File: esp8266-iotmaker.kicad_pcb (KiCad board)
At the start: 2 copper layers, 66.3 x 30.7 mm, 70 parts, among them J1 CONN_01X04, J2 CONN_01X02, J3 CONN_01X08, J4 CONN_01X06, J5 CONN_01X08, J6 CONN_01X04, Q1 S8050, Q2 S8050, SW1 SW_Push, SW2 SW_Push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

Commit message: complete pcb source
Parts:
- removed C19, C20, C21, C22: C, esp8266:C_0603
- C12, C14: value C -> 10uF; footprint esp8266:C_0603 -> Capacitors_SMD:CP_Elec_4x5.3
- C15, C18: value C -> 22uF; footprint esp8266:C_0603 -> Capacitors_SMD:CP_Elec_4x5.3
- D5: footprint esp8266:do214aa-g -> Diodes_SMD:D_SOD-323
- D7: footprint Diodes_SMD:D_SOD-123 -> Diodes_SMD:D_SOD-323
- SW1, SW2: footprint esp8266:Tact_Switch_TS6X3.6 -> esp8266:micro-buttom
- moved D4 76.5 mm to (90.8, 124.1)
- moved L1 68.8 mm to (121.2, 123.0), turned to 0 degrees
- moved C2 68.8 mm to (121.2, 123.0), turned to 0 degrees
- moved C14 67.4 mm to (99.2, 126.4), turned to 90 degrees
- moved C1 67.1 mm to (121.2, 123.0), turned to 0 degrees
- moved L2 65.9 mm to (121.2, 123.0)
- moved C3 65.6 mm to (121.2, 123.0), turned to 0 degrees
- moved R20 65.0 mm to (121.2, 123.0), turned to 0 degrees
- moved C4 64.4 mm to (121.2, 123.0)
- moved R13 64.1 mm to (121.2, 123.0), turned to 0 degrees
- moved C5 63.7 mm to (121.2, 123.0), turned to 0 degrees
- moved Y1 63.7 mm to (121.2, 123.0), turned to 0 degrees
- moved R12 62.5 mm to (121.2, 123.0), turned to 0 degrees
- moved C7 61.3 mm to (121.2, 123.0), turned to 0 degrees
- moved D2 60.3 mm to (121.2, 123.0), turned to 0 degrees
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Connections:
- C14 pad 1: VBAT -> Net-(C14-Pad1)
- C15 pad 1: Net-(C15-Pad1) -> 3V3
- C18 pad 1: Net-(C15-Pad1) -> 5V
- D4 pad 1: Net-(C15-Pad1) -> Net-(C14-Pad1)
- D5 pad 1: Net-(C15-Pad1) -> Net-(C14-Pad1)
- U7 pad 3: Net-(C15-Pad1) -> Net-(C14-Pad1)
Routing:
- net GND: track 325.7 -> 50.3 mm, vias 14 -> 0
- net 3V3: track 174.2 -> 6.35 mm, vias 8 -> 1
- net REST: track 80.4 -> 0.00 mm, vias 1 -> 0
- net GPIO16: track 72.7 -> 0.00 mm, vias 2 -> 0
- net VBAT: track 74.8 -> 4.18 mm, vias 2 -> 0
- net TXD: track 61.7 -> 0.00 mm, vias 2 -> 0
- net GPIO0: track 56.2 -> 0.00 mm, vias 3 -> 0
- net RXD: track 51.7 -> 0.00 mm, vias 2 -> 0
- net EN: track 42.1 -> 0.00 mm, vias 2 -> 0
- net MOSI: track 38.4 -> 0.00 mm, vias 1 -> 0
- net GPIO14: track 37.6 -> 0.00 mm, vias 1 -> 0
- net CSO: track 37.2 -> 0.00 mm, vias 1 -> 0
- net GPIO12: track 34.0 -> 0.00 mm, vias 1 -> 0
- net GPIO13: track 30.8 -> 0.00 mm, vias 1 -> 0
- net GPIO15: track 28.9 -> 0.00 mm, vias 1 -> 0
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- removed copper zone on B.Cu, net GND
- removed copper zone on F.Cu, net GND
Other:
- board size 66.3 x 30.7 mm -> 50.8 x 25.4 mm
- net class Default: trace_width 0.254 -> 0.2; via_dia 1.1 -> 1; via_drill 0.6 -> 0.5

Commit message: xap xep linh kien
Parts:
- removed BT1: Battery, Pin_Headers:Pin_Header_Straight_2x01_Pitch2.00mm
- removed C14: 10uF, Capacitors_SMD:CP_Elec_4x5.3
- removed C16: 4.7uF, esp8266:C_0603
- removed C17: 1uF, esp8266:C_0603
- removed C18: 22uF, Capacitors_SMD:CP_Elec_4x5.3
- removed D2: ZENER_3V3, Diodes_SMD:D_SOD-323_HandSoldering
- removed D4: SS34, esp8266:do214aa-g
- removed D7: BAT60JFILM, Diodes_SMD:D_SOD-323
- removed J3, J5: CONN_01X08, Pin_Headers:Pin_Header_Straight_1x08_Pitch2.54mm
- removed J4: CONN_01X06, Pin_Headers:Pin_Header_Straight_1x06_Pitch2.54mm
- removed J6: CONN_01X04, Pin_Headers:Pin_Header_Straight_1x04_Pitch2.54mm
- removed R17: 2K, esp8266:R_0603
- removed R19: 100k, esp8266:R_0603
- removed U5: mcp73831, TO_SOT_Packages_SMD:SOT-23-5
- removed U7: AMS1117-3.3, TO_SOT_Packages_SMD:SOT-223
- removed U8: MOSFET-P, esp8266:SOT-23_standar
- C12: value 10uF -> 10uF TANT; footprint Capacitors_SMD:CP_Elec_4x5.3 -> Capacitors_SMD:C_1206
- C13: value 4.7uF -> 100nF
- C15: value 22uF -> 10uF TANT; footprint Capacitors_SMD:CP_Elec_4x5.3 -> Capacitors_SMD:C_1206
- D5: value SS34 -> 1n5819; footprint Diodes_SMD:D_SOD-323 -> Diodes_SMD:D_SOD-123
- J1: value CONN_01X04 -> CONN_01X10; footprint Pin_Headers:Pin_Header_Straight_1x04_Pitch2.54mm -> Pin_Headers:Pin_Header_Straight_1x10_Pitch2.54mm
- J2: value CONN_01X02 -> CONN_01X10; footprint Pin_Headers:Pin_Header_Straight_1x02_Pitch2.54mm -> Pin_Headers:Pin_Header_Straight_1x10_Pitch2.54mm
- SW1, SW2: footprint esp8266:micro-buttom -> esp8266:tactile switches
- U3: footprint Housings_DFN_QFN:QFN-28-1EP_5x5mm_Pitch0.5mm -> esp8266:cp2102
- U4: footprint Housings_SOIC:SOIJ-8_5.3x5.3mm_Pitch1.27mm -> Housings_SOIC:SOIC-8_3.9x4.9mm_Pitch1.27mm
- moved R8 60.6 mm to (118.6, 62.5), turned to 180 degrees
- moved R4 59.0 mm to (118.6, 64.0), turned to 180 degrees
- moved R15 57.6 mm to (118.6, 65.5), turned to 180 degrees
- moved R5 56.1 mm to (118.6, 66.9), turned to 180 degrees
- moved C15 51.9 mm to (96.8, 77.2), turned to 180 degrees
- moved L1 50.9 mm to (136.2, 74.3)
- moved D1 50.4 mm to (95.0, 79.9), turned to 270 degrees
- moved R11 49.7 mm to (96.4, 79.9), turned to 270 degrees
- moved C2 49.6 mm to (134.2, 75.1), turned to 90 degrees
- moved R7 49.4 mm to (145.5, 79.9)
- moved L2 49.3 mm to (136.2, 76.0)
- moved C3 49.3 mm to (132.7, 75.1), turned to 90 degrees
- moved C1 49.0 mm to (131.4, 75.1), turned to 90 degrees
- moved R12 48.7 mm to (129.8, 75.1), turned to 270 degrees
- moved R13 48.4 mm to (128.3, 75.1), turned to 90 degrees
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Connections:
- C12 pad 1: VBAT -> VCC
- C13 pad 1: 5V -> 3V3
- C6 pad 1: VUSB -> VCC
- C8 pad 1: VUSB -> VCC
- D5 pad 1: Net-(C14-Pad1) -> VCC
- J1 pad 1: GPIO16 -> GPIO14
- J1 pad 2: ADC_EX -> GPIO12
- J1 pad 3: GND -> GPIO13
- J1 pad 4: 3V3 -> GPIO15
- J2 pad 1: GPIO2 -> GPIO16
- J2 pad 2: GPIO0 -> ADC_EX
- U3 pad 29: (no net) -> GND
- U3 pad 8: VUSB -> VCC
- U4 pad 8: GND -> 3V3
- U6 pad 3: VBAT -> VCC
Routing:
- net GND: track 50.3 -> 16.3 mm, vias 0 -> 1
- net VCC: track 0.00 -> 24.3 mm
- net MOSI: track 0.00 -> 22.2 mm
- net Net-(BT1-Pad1): track 19.0 -> 0.00 mm
- net D-: track 1.05 -> 15.9 mm, vias 1 -> 2
- net D+: track 1.09 -> 15.0 mm, vias 1 -> 2
- net 3V3: track 6.35 -> 18.2 mm, vias 1 -> 0
- net GPIO9: track 0.00 -> 10.6 mm
- net 5V: track 10.1 -> 0.00 mm
- net TXD: track 0.00 -> 9.74 mm
- net RXD: track 0.00 -> 9.68 mm
- net Net-(C7-Pad2): track 0.00 -> 9.32 mm
- net VUSB: track 13.3 -> 4.54 mm
- net Net-(R3-Pad1): track 0.00 -> 8.49 mm
- net MISO: track 0.00 -> 7.89 mm
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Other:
- board outline removed

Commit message: complete pcb ver2.0
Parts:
- SW1, SW2: footprint esp8266:tactile switches -> esp8266:nut_nhan_ngang
- moved R14 40.2 mm to (98.1, 74.8), turned to 270 degrees
- moved C13 39.7 mm to (119.4, 91.6), turned to 90 degrees
- moved R15 32.6 mm to (97.5, 90.4)
- moved R8 24.3 mm to (107.5, 84.0)
- moved R7 21.8 mm to (128.9, 94.1), turned to 270 degrees
- moved R3 20.7 mm to (112.4, 91.4), turned to 270 degrees
- moved C11 18.6 mm to (129.5, 91.0), turned to 90 degrees
- moved AE1 16.6 mm to (129.7, 79.0), turned to 270 degrees
- moved R4 15.7 mm to (109.8, 77.0)
- moved C7 15.2 mm to (122.5, 93.3), turned to 90 degrees
- moved U4 15.0 mm to (116.0, 90.0), turned to 270 degrees
- moved Y1 14.9 mm to (125.0, 93.3), turned to 90 degrees
- moved R6 14.6 mm to (112.9, 79.6), turned to 180 degrees
- moved R5 14.6 mm to (109.8, 78.5)
- moved R12 12.3 mm to (117.9, 78.2)
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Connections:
- J2 pad 1: GPIO16 -> GND
- J2 pad 10: GND -> REST
- J2 pad 2: ADC_EX -> GND
- J2 pad 3: GND -> VCC
- J2 pad 5: EN -> GPIO0
- J2 pad 6: REST -> GPIO2
- J2 pad 7: GPIO0 -> GPIO16
- J2 pad 8: GPIO2 -> EN
- J2 pad 9: VUSB -> ADC_EX
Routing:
- net GND: track 16.3 -> 236.2 mm, vias 1 -> 14
- net 3V3: track 18.2 -> 146.5 mm, vias 0 -> 11
- net REST: track 0.00 -> 101.6 mm, vias 0 -> 5
- net GPIO0: track 1.29 -> 66.8 mm, vias 1 -> 2
- net GPIO16: track 3.23 -> 50.5 mm, vias 0 -> 2
- net GPIO15: track 0.00 -> 46.1 mm, vias 0 -> 1
- net GPIO14: track 0.00 -> 32.4 mm
- net GPIO12: track 0.00 -> 29.3 mm
- net GPIO2: track 0.00 -> 27.8 mm, vias 0 -> 1
- net DTR: track 2.67 -> 28.4 mm, vias 1 -> 0
- net GPIO13: track 0.00 -> 25.5 mm
- net TXD: track 9.74 -> 33.6 mm, vias 0 -> 1
- net GPIO4: track 0.00 -> 23.5 mm, vias 0 -> 1
- net RXD: track 9.68 -> 32.7 mm, vias 0 -> 1
- net EN: track 0.00 -> 17.2 mm
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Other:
- board outline added: 50.8 x 26.2 mm
- net class Default: clearance 0.2 -> 0.254
- rule trace_clearance: 0.2 -> 0.254

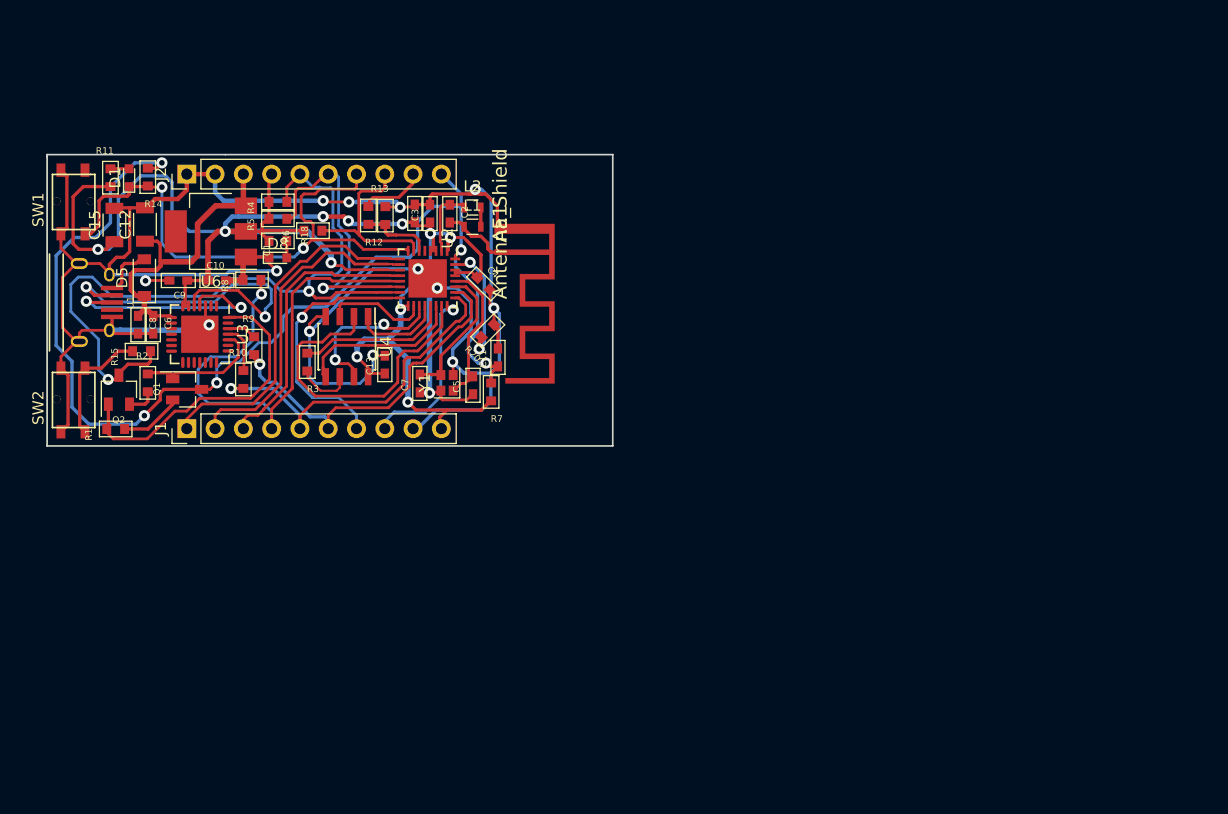
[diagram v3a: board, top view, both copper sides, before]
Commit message: add 3d and edit pcb
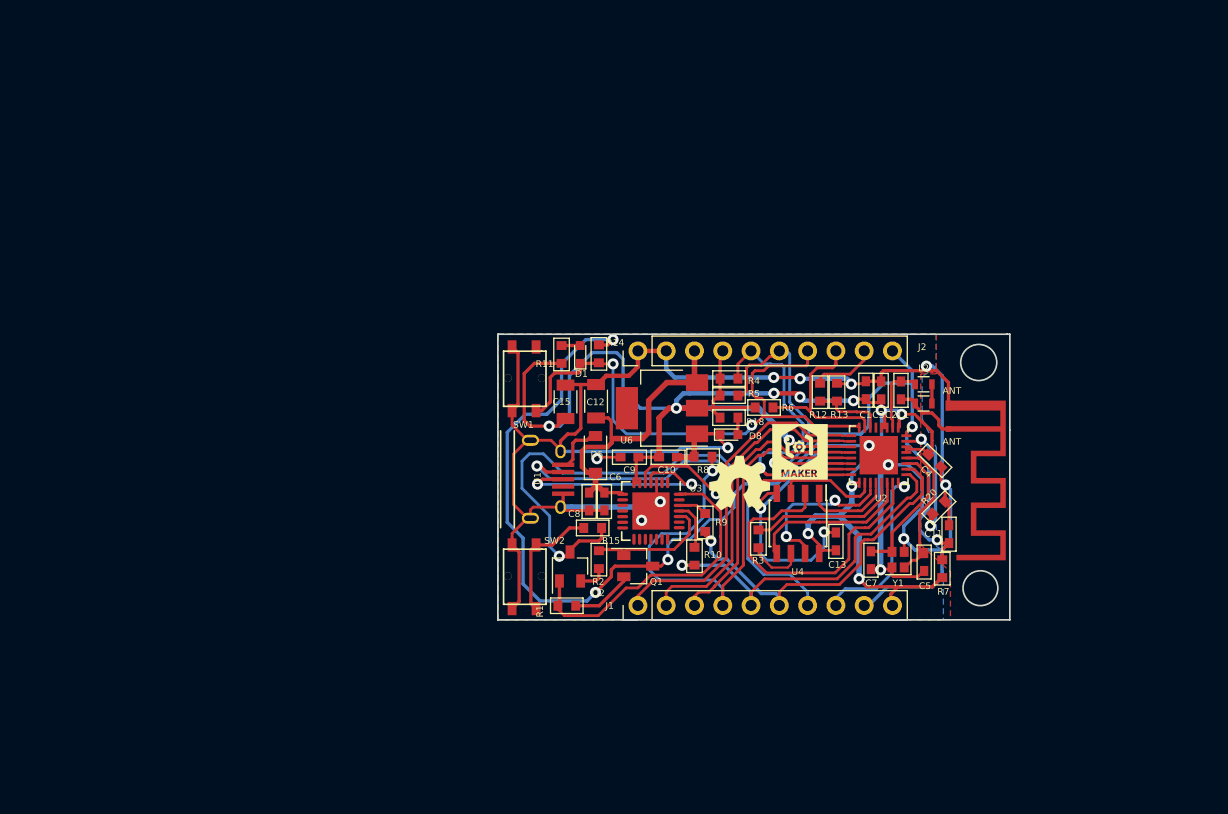
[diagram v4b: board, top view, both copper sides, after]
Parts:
- added G***: LOGO, esp8266:logo_cc-bby-sa_14.1x5mm, B.Cu at (153.6, 101.8)
- added G***: LOGO, esp8266:logo_openhardware_5x5mm, F.Cu at (151.2, 102.3)
- added G***: LOGO, esp8266:logo-iotmaker-v1, F.Cu at (156.7, 99.5)
- added G***: LOGO, esp8266:logo-iotmakervn_7.5x5, B.Cu at (141.9, 101.7)
- added G***: LOGO, esp8266:logo_openhardware_5x5mm, B.Cu at (163.9, 101.8)
- ANT: renamed from AE1; value Antenna_Shield -> ANT
- moved R12 43.6 mm to (158.5, 94.1)
- moved R13 43.6 mm to (160.0, 94.1)
- moved C2 43.5 mm to (165.7, 93.9)
- moved C11 43.5 mm to (170.1, 106.9)
- moved C12 43.5 mm to (138.4, 94.9)
- moved C13 43.5 mm to (159.9, 107.5)
- moved C15 43.5 mm to (135.6, 95.0)
- moved C4 43.5 mm to (168.8, 100.3)
- moved C5 43.5 mm to (167.8, 109.4)
- moved C6 43.5 mm to (139.1, 103.9)
- moved C8 43.5 mm to (137.7, 103.9)
- moved C9 43.5 mm to (141.4, 99.9)
- moved J1 43.5 mm to (142.1, 113.3)
- moved J2 43.5 mm to (142.1, 90.4)
- moved Q1 43.5 mm to (142.1, 109.7)
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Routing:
- net GPIO2: track 27.8 -> 30.0 mm
- net GPIO0: track 66.8 -> 67.8 mm
- net GPIO13: track 25.5 -> 26.0 mm
- net GND: track 236.2 -> 236.6 mm, vias 14 -> 15
- added copper zone on B.Cu, net GND
- added copper zone on F.Cu, net GND
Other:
- board size 50.8 x 26.2 mm -> 46 x 25.7 mm
- board text added: "3V3"
- board text added: "ADC_IN"
- board text added: "Designed by IoTMakerVn"
- board text added: "ENABLE"
- board text added: "GND"
- board text added: "GPIO0"
- board text added: "GPIO02"
- board text added: "GPIO12"
- board text added: "GPIO13"
- board text added: "GPIO14"
- board text added: "GPIO15"
- board text added: "GPIO16"
- board text added: "GPIO4"
- board text added: "GPIO5"
- board text added: "RESET"
- board text added: "RXD"
- board text added: "TXD"
- board text added: "VCC"

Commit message: edit solder mark
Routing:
- net GPIO14: track 32.4 -> 33.3 mm
- added copper zone on F.Cu, net 3V3

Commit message: edit pcb
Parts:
- moved ANT 0.51 mm to (170.3, 94.4)
- moved L1 0.11 mm to (167.9, 95.1)
- moved L2 0.11 mm to (167.9, 93.4)
- moved U6 0.07 mm to (144.3, 95.5)
- moved Q1 0.05 mm to (142.2, 109.7)
- moved C2 0.05 mm to (165.8, 94.0)
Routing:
- net 3V3: track 146.2 -> 153.8 mm
- net GND: track 236.6 -> 231.6 mm
- net REST: track 101.6 -> 96.7 mm
- net GPIO16: track 50.8 -> 46.6 mm
- net GPIO2: track 30.0 -> 27.8 mm
- net GPIO15: track 46.6 -> 44.7 mm
- net GPIO4: track 23.5 -> 21.7 mm
- net RXD: track 32.7 -> 31.1 mm
- net VCC: track 28.4 -> 29.6 mm
- net EN: track 16.9 -> 15.7 mm
- net Net-(U6-Pad4): track 1.13 -> 0.00 mm
- net GPIO0: track 67.8 -> 66.9 mm
- net GPIO10: track 14.6 -> 13.6 mm
- net TXD: track 33.6 -> 32.9 mm
- net ADC_EX: track 5.99 -> 5.32 mm
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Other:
- net class Default: trace_width 0.2 -> 0.254
- board text added: "ADC"
- board text added: "EN"
- board text added: "IO0"
- board text added: "IO02"
- board text added: "IO04"
- board text added: "IO05"
- board text added: "IO12"
- board text added: "IO13"
- board text added: "IO14"
- board text added: "IO15"
- board text added: "IO16"
- board text added: "RST"

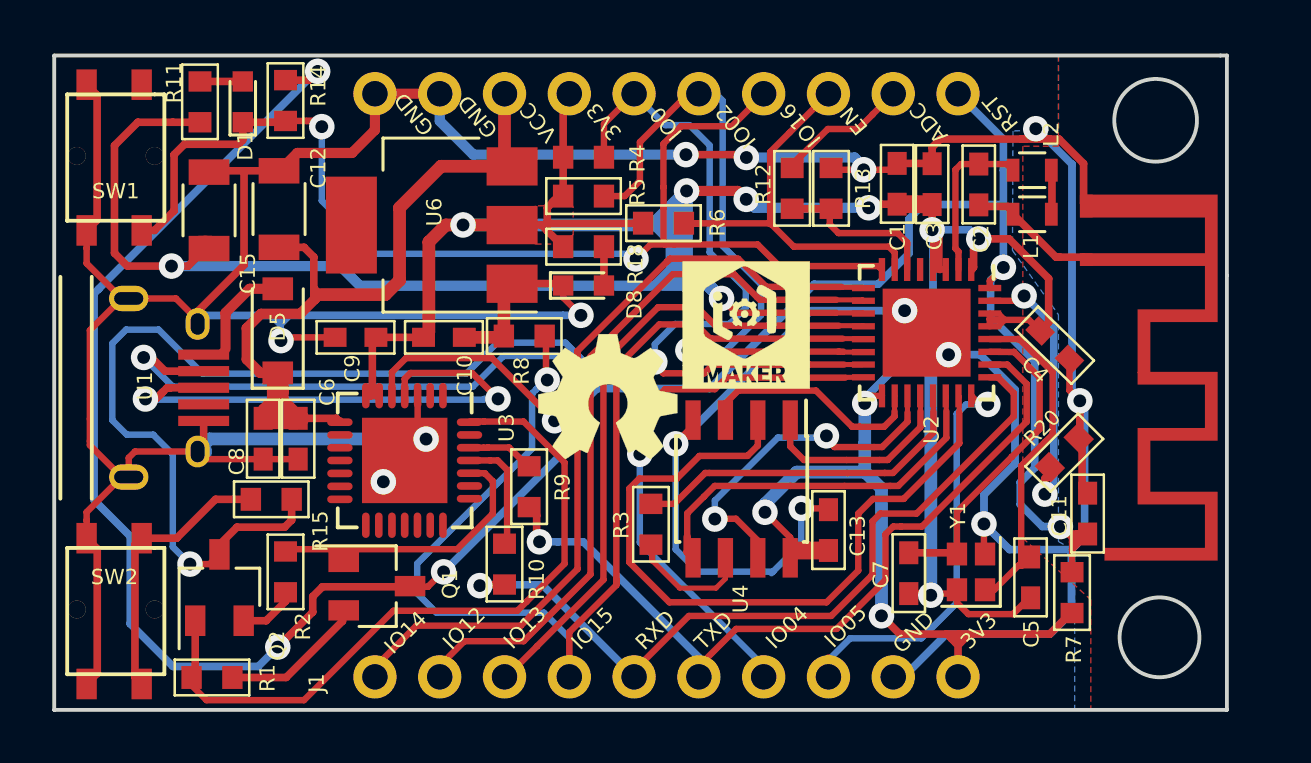
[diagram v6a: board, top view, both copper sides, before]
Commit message: edit pcb with new crystal
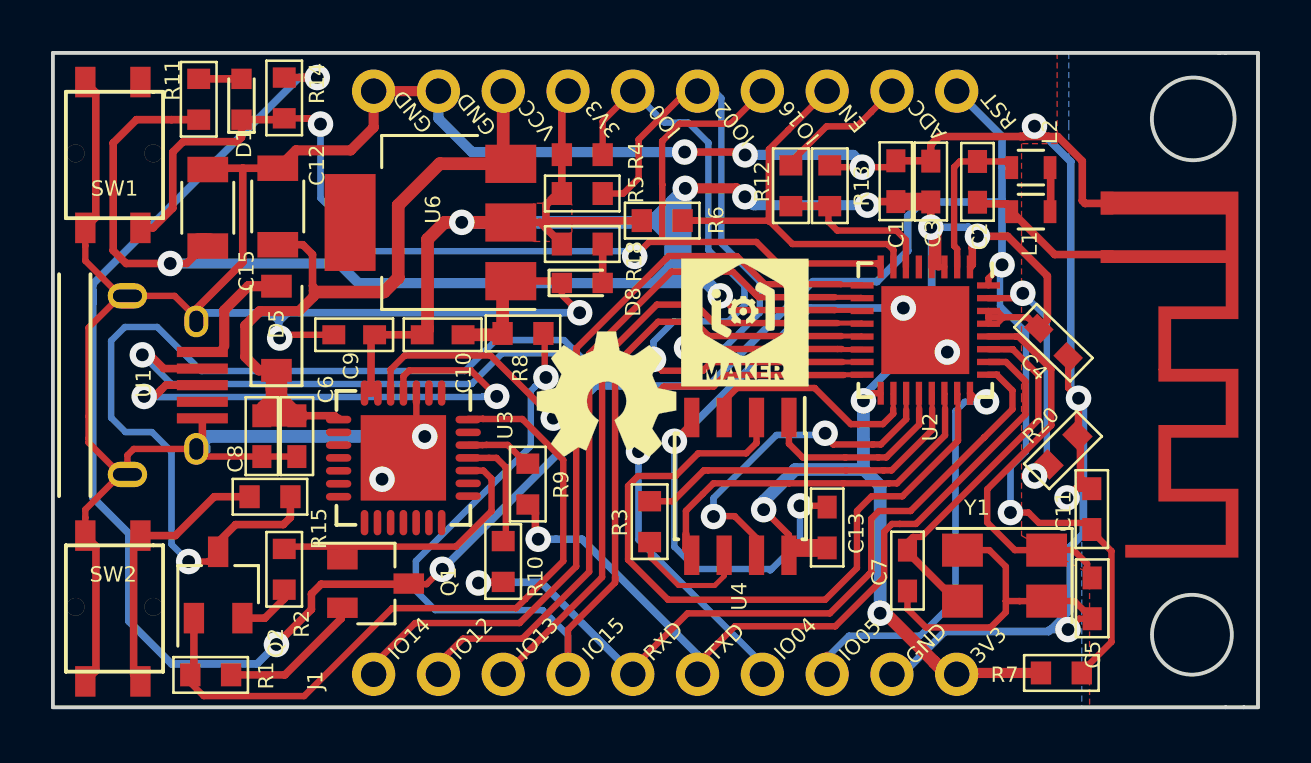
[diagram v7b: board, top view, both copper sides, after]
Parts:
- Y1: footprint Crystals:Crystal_SMD_2016-4pin_2.0x1.6mm -> Crystals:Crystal_SMD_5032-4pin_5.0x3.2mm
- moved R7 3.18 mm to (169.0, 113.1), turned to 180 degrees
- moved C5 2.55 mm to (170.2, 110.2)
- moved Y1 1.32 mm to (166.8, 109.3), turned to 180 degrees
- moved ANT 0.82 mm to (171.1, 94.2)
- moved C11 0.24 mm to (170.2, 106.7)
- moved C15 0.11 mm to (135.6, 94.9)
- moved C9 0.11 mm to (141.3, 99.8)
- moved D1 0.11 mm to (136.9, 90.6)
- moved G*** 0.11 mm to (153.5, 101.7)
- moved G*** 0.11 mm to (141.9, 101.5)
- moved J1 0.11 mm to (142.1, 113.2)
- moved J2 0.11 mm to (142.1, 90.3)
- moved Q1 0.11 mm to (142.1, 109.6)
- moved R10 0.11 mm to (147.1, 108.7)
- moved R11 0.11 mm to (135.2, 90.6)
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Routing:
- net GND: track 231.6 -> 219.0 mm
- net REST: track 96.7 -> 101.2 mm
- net 3V3: track 153.8 -> 150.2 mm
- net Net-(C7-Pad2): track 12.6 -> 14.7 mm
- net Net-(C5-Pad2): track 13.6 -> 15.3 mm
- net Net-(AE1-Pad1): track 5.17 -> 6.03 mm
- net Net-(R20-Pad2): track 11.0 -> 10.2 mm
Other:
- board size 46 x 25.7 mm -> 47.2 x 25.7 mm
